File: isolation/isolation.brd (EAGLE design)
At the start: 74.5 x 72.7 mm, 90 parts, among them IC1 XTLV61048DBVR, IC2 SN74HC14PWR, IC3 SN74HCS32BQAR, IC4 SN74HCS08DYYR, IC5 FDN359BN, IC6 FDN359BN, IC7 FDN359BN, IC8 FDN359BN, J1 S4B-PH-K-S(LF)(SN), J2 S4B-PH-K-S(LF)(SN), J3 S2B-PH-K-S(LF)(SN), J4 S2B-PH-K-S(LF)(SN), J5 S2B-PH-K-S(LF)(SN), J6 USBC

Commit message: fix drc issues
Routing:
- net FIRE2: track 38.0 -> 39.7 mm
- net N$24: track 8.36 -> 7.42 mm
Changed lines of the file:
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@@
 <setting verticaltext="up"/>
 </settings>
-<grid distance="50" unitdist="mil" unit="mil" style="lines" multiple="1" display="no" altdistance="5" altunitdist="mil" altunit="mil"/>
+<grid distance="1" unitdist="mm" unit="mm" style="lines" multiple="1" display="no" altdistance="0.1" altunitdist="mm" altunit="mm"/>
 <layers>
 <layer number="1" name="Top" color="4" fill="1" visible="yes" active="yes"/>
@@
 <text x="5" y="-33" size="3" layer="22" font="vector" ratio="15" rot="MR0">Lockie</text>
 <text x="14.969" y="10.376" size="2" layer="22" font="vector" ratio="15" rot="MR0">Designed by ART Avionics</text>
-<text x="12.029" y="12.595" size="1.5" layer="22" font="vector" ratio="15" rot="MR0">Shrey Bohra</text>
+<text x="11.029" y="12.595" size="1.1" layer="22" font="vector" ratio="15" rot="MR0">Shrey Bohra</text>
 <text x="11.358" y="14.786" size="1" layer="22" font="vector" ratio="15" rot="MR0">Shreya Ramteke Sharwa Molla</text>
 <text x="3.598" y="16.306" size="1" layer="22" font="vector" ratio="15" rot="MR0">Abhik Chatterjee</text>
 <text x="4.066" y="18.493" size="1" layer="22" font="vector" ratio="15" rot="MR0">Camillo De Gregorio</text>
-<text x="-0.346" y="12.728" size="1" layer="22" font="vector" ratio="15" rot="MR0">Simeon Charles</text>
+<text x="0.654" y="12.728" size="1" layer="22" font="vector" ratio="15" rot="MR0">Simeon Charles</text>
 <text x="-18.415" y="19.685" size="1" layer="22" font="vector" ratio="15" rot="MR0">GND</text>
 <text x="-21.971" y="17.018" size="1" layer="22" font="vector" ratio="15" rot="MR0">VCC</text>
@@
 <text x="31.75" y="3.175" size="1.5" layer="21" font="vector" ratio="15" rot="R270">USB C</text>
 <text x="2.794" y="-22.606" size="1" layer="21" font="vector" ratio="15">JLCJLCJLCJLC</text>
+<text x="16.03" y="-29.21" size="1" layer="22" font="vector" ratio="12" rot="MR0">VCC</text>
+<text x="-16.57294375" y="-18.11725" size="1" layer="22" font="vector" ratio="12" rot="MR60">Raven Input</text>
+<text x="14.758228125" y="-18.887253125" size="1" layer="22" font="vector" ratio="12" rot="MR120">Pickle Input</text>
 </plain>
 <attributes>
@@
 <wire x1="-19.7358" y1="21.8694" x2="-19.67" y2="21.861" width="0.1524" layer="16"/>
 <wire x1="-16.5354" y1="24.3586" x2="-16.51" y2="24.5236" width="0.1524" layer="1"/>
-<wire x1="-17.4244" y1="22.7584" x2="-18.3134" y2="21.8694" width="0.1524" layer="16"/>
-<wire x1="-17.4244" y1="23.4696" x2="-17.4244" y2="22.7584" width="0.1524" layer="16"/>
-<wire x1="-18.3134" y1="21.8694" x2="-18.37" y2="21.861" width="0.1524" layer="16"/>
+<wire x1="-18.1244" y1="22.7584" x2="-18.37" y2="22.5128" width="0.1524" layer="16"/>
+<wire x1="-18.37" y1="21.861" x2="-18.37" y2="22.5128" width="0.1524" layer="16"/>
+<wire x1="-17.9578" y1="24.003" x2="-18.1244" y2="23.8364" width="0.1524" layer="16"/>
+<wire x1="-18.1244" y1="23.8364" x2="-18.1244" y2="22.7584" width="0.1524" layer="16"/>
 <wire x1="-13.208" y1="19.177" x2="-12.7" y2="19.685" width="0.1524" layer="16"/>
 <wire x1="-12.7" y1="20.05555" x2="-12.7" y2="19.685" width="0.1524" layer="16"/>
@@
 <wire x1="-12.0904" y1="16.891" x2="-11.954" y2="16.778" width="0.1524" layer="16"/>
 <wire x1="-12.446" y1="16.891" x2="-12.454" y2="16.778" width="0.1524" layer="16"/>
-<wire x1="-17.9578" y1="24.003" x2="-17.4244" y2="23.4696" width="0.1524" layer="16"/>
 <wire x1="-19.0246" y1="23.2918" x2="-19.05" y2="23.25335" width="0.1524" layer="1"/>
 <wire x1="9.001" y1="5.08" x2="11.43" y2="7.62" width="0.1524" layer="16"/>
@@
 <wire x1="-12.0904" y1="12.9794" x2="-11.9126" y2="13.1572" width="0.1524" layer="16"/>
 <wire x1="-11.7348" y1="12.6238" x2="-12.0904" y2="12.9794" width="0.1524" layer="16"/>
-<wire x1="-12.446" y1="11.9126" x2="-11.9126" y2="12.446" width="0.1524" layer="16"/>
-<wire x1="-11.9126" y1="12.446" x2="-11.7348" y2="12.6238" width="0.1524" layer="16"/>
+<wire x1="-12.446" y1="11.9126" x2="-11.8626" y2="12.496" width="0.1524" layer="16"/>
+<wire x1="-11.8626" y1="12.496" x2="-11.7348" y2="12.6238" width="0.1524" layer="16"/>
 <wire x1="-15.113" y1="11.9126" x2="-13.97" y2="11.9126" width="0.1524" layer="16"/>
 <wire x1="-13.97" y1="11.9126" x2="-12.446" y2="11.9126" width="0.1524" layer="16"/>
@@
 <wire x1="-11.9126" y1="13.6906" x2="-11.954" y2="13.702" width="0.1524" layer="16"/>
 <wire x1="-32.5374" y1="8.1788" x2="-32.385" y2="8.348" width="0.1524" layer="1"/>
-<wire x1="-11.3792" y1="11.9126" x2="-11.9126" y2="12.446" width="0.1524" layer="16"/>
-<wire x1="-10.1346" y1="10.668" x2="-11.3792" y2="11.9126" width="0.1524" layer="1"/>
+<wire x1="-11.1792" y1="11.8126" x2="-11.8626" y2="12.496" width="0.1524" layer="16"/>
+<wire x1="-10.1346" y1="10.668" x2="-10.1346" y2="10.768" width="0.1524" layer="1"/>
+<wire x1="-10.1346" y1="10.768" x2="-11.1792" y2="11.8126" width="0.1524" layer="1"/>
 <wire x1="-10.1346" y1="7.3406" x2="-10.1346" y2="10.668" width="0.1524" layer="16"/>
 <wire x1="-10.1346" y1="7.112" x2="-10.1346" y2="7.3406" width="0.1524" layer="1"/>
@@
 <via x="-20.8026" y="17.78" extent="1-16" drill="0.35"/>
 <via x="-19.9136" y="18.669" extent="1-16" drill="0.35"/>
-<via x="-11.3792" y="11.9126" extent="1-16" drill="0.35"/>
+<via x="-11.1792" y="11.8126" extent="1-16" drill="0.35"/>
 <via x="-10.1346" y="10.668" extent="1-16" drill="0.35"/>
 <via x="-10.1346" y="7.3406" extent="1-16" drill="0.35"/>
@@
 <wire x1="-28.448" y1="8.1788" x2="-28.448" y2="8.348" width="0.1524" layer="1"/>
 <wire x1="-28.3972" y1="16.3576" x2="-28.448" y2="16.51" width="0.1524" layer="16"/>
-<wire x1="-12.8016" y1="9.779" x2="-11.7348" y2="9.779" width="0.1524" layer="1"/>
+<wire x1="-11.684" y1="9.8322" x2="-11.8016" y2="9.9498" width="0.1524" layer="1"/>
+<wire x1="-11.8016" y1="9.9498" x2="-11.8016" y2="11.079" width="0.1524" layer="1"/>
 <wire x1="-14.4018" y1="8.1788" x2="-13.335" y2="9.2456" width="0.1524" layer="16"/>
-<wire x1="-13.335" y1="9.2456" x2="-12.8016" y2="9.779" width="0.1524" layer="16"/>
+<wire x1="-13.485" y1="9.3956" x2="-11.8016" y2="11.079" width="0.1524" layer="16"/>
 <wire x1="-27.2034" y1="8.1788" x2="-14.4018" y2="8.1788" width="0.1524" layer="16"/>
-<wire x1="-11.7348" y1="9.779" x2="-11.684" y2="9.8322" width="0.1524" layer="1"/>
 <via x="-27.2034" y="7.0866" extent="1-16" drill="0.35"/>
-<via x="-12.8016" y="9.779" extent="1-16" drill="0.35"/>
+<via x="-11.8016" y="11.079" extent="1-16" drill="0.35"/>
 <wire x1="-14.0462" y1="12.9794" x2="-14.0462" y2="13.6906" width="0.1524" layer="16"/>
 <wire x1="-14.4018" y1="12.6238" x2="-14.0462" y2="12.9794" width="0.1524" layer="16"/>
@@
 <wire x1="-15.8242" y1="12.0904" x2="-15.2908" y2="12.6238" width="0.1524" layer="16"/>
 <wire x1="-15.8242" y1="11.7348" x2="-15.8242" y2="12.0904" width="0.1524" layer="16"/>
-<wire x1="-13.335" y1="9.2456" x2="-15.8242" y2="11.7348" width="0.1524" layer="16"/>
+<wire x1="-13.335" y1="9.2456" x2="-13.485" y2="9.3956" width="0.1524" layer="16"/>
+<wire x1="-13.485" y1="9.3956" x2="-15.8242" y2="11.7348" width="0.1524" layer="16"/>
 <wire x1="-14.0462" y1="13.6906" x2="-13.954" y2="13.702" width="0.1524" layer="16"/>
 </signal>
@@
 <contactref element="J6" pad="B5"/>
 <contactref element="R12" pad="1"/>
-<wire x1="27.66795" y1="6.78675" x2="27.9932" y2="7.112" width="0.1524" layer="1"/>
 <via x="26.416" y="5.207" extent="1-16" drill="0.35"/>
 <wire x1="26.416" y1="5.207" x2="26.797" y2="4.826" width="0.1524" layer="16"/>
@@
 <wire x1="28.28" y1="2.131" x2="28.181" y2="2.032" width="0.1524" layer="1"/>
 <wire x1="28.181" y1="2.032" x2="26.797" y2="2.032" width="0.1524" layer="1"/>
-<wire x1="27.9932" y1="7.112" x2="27.806196875" y2="6.924996875" width="0.1778" layer="1"/>
-<wire x1="27.9932" y1="6.4032" x2="26.797" y2="5.207" width="0.1778" layer="1"/>
-<wire x1="26.416" y1="5.207" x2="26.797" y2="5.207" width="0.1778" layer="1"/>
-<wire x1="27.9932" y1="6.4032" x2="27.9932" y2="7.112" width="0.1778" layer="1"/>
+<wire x1="26.416" y1="5.207" x2="27.9932" y2="6.7842" width="0.1778" layer="1"/>
+<wire x1="27.9932" y1="6.7842" x2="27.9932" y2="7.112" width="0.1778" layer="1"/>
 </signal>
 <signal name="N$25">
@@
 <wire x1="-11.0236" y1="21.5138" x2="-11.7348" y2="21.5138" width="0.1524" layer="16"/>
 <wire x1="-10.8458" y1="21.336" x2="-11.0236" y2="21.5138" width="0.1524" layer="16"/>
-<wire x1="-16.5354" y1="21.336" x2="-10.8458" y2="21.336" width="0.1524" layer="1"/>
+<wire x1="-11.0458" y1="21.536" x2="-10.8458" y2="21.336" width="0.1524" layer="1"/>
+<wire x1="-11.0458" y1="21.536" x2="-16.3354" y2="21.536" width="0.1524" layer="1"/>
 <wire x1="-17.1958" y1="21.7424" x2="-16.6624" y2="21.209" width="0.1524" layer="1"/>
 <wire x1="-17.1958" y1="27.9654" x2="-17.1958" y2="21.7424" width="0.1524" layer="16"/>
@@
 <wire x1="-17.7038" y1="19.1008" x2="-18.0594" y2="19.1008" width="0.1524" layer="16"/>
 <wire x1="-17.7038" y1="20.1676" x2="-17.7038" y2="19.1008" width="0.1524" layer="1"/>
-<wire x1="-16.5354" y1="21.336" x2="-16.6624" y2="21.209" width="0.1524" layer="1"/>
+<wire x1="-16.3354" y1="21.536" x2="-16.6624" y2="21.209" width="0.1524" layer="1"/>
 <wire x1="-16.6624" y1="21.209" x2="-17.7038" y2="20.1676" width="0.1524" layer="1"/>
 <wire x1="-19.7358" y1="16.002" x2="-19.67" y2="15.985" width="0.1524" layer="16"/>

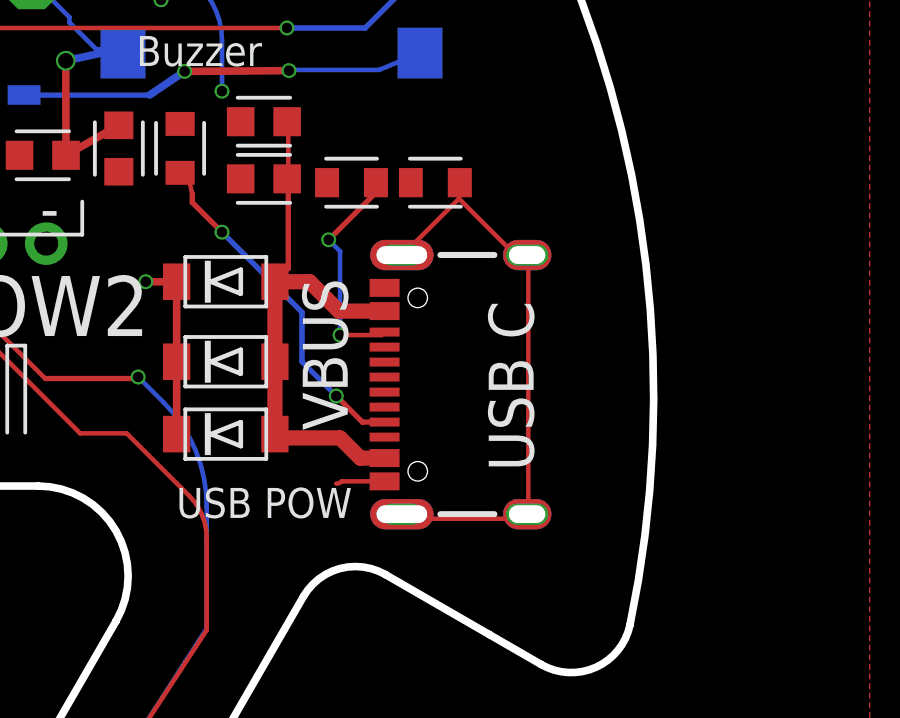
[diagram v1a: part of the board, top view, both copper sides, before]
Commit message: swap usb c connector
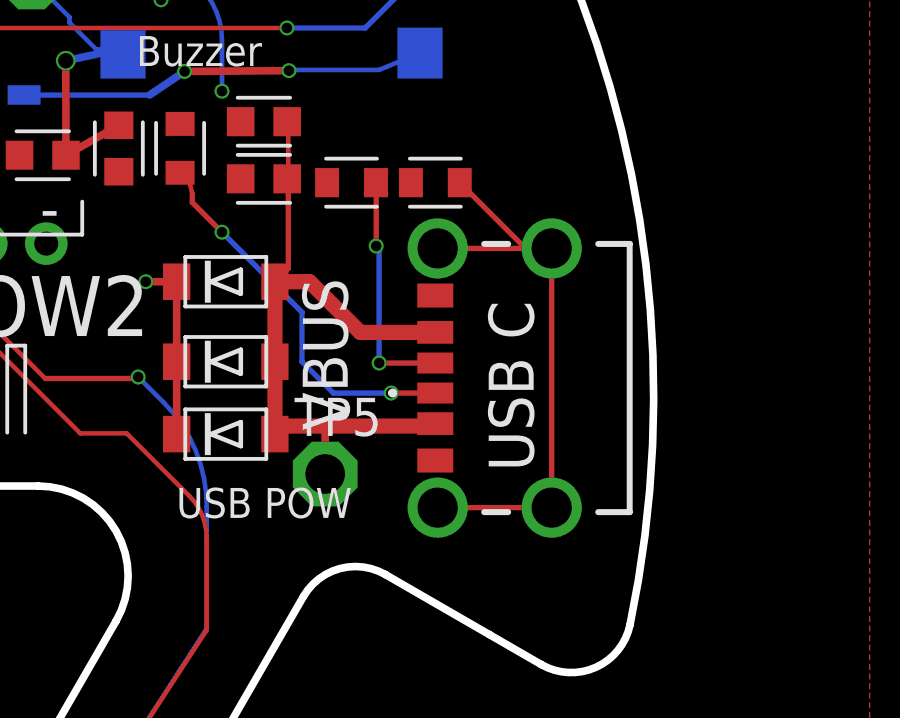
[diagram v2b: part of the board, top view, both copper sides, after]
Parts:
- removed J6: USBC, SparkFun-Connectors:USB-C-16P-2LAYER-PADS
- added J7: 217175-0001, SamacSys_Parts:2171750001
- added TP5: PTR1PAD1-13, testpad:P1-13
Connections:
- removed net N$21: J6.SHLD1, J6.SHLD2, J6.SHLD3, J6.SHLD4, R13.1
- removed net N$24: J6.B5, R12.1
- removed net N$25: J6.A5, R14.1
- removed net N$26: C14.2, C15.2, D2.A, D3.A, D4.A, J6.VBUS1, J6.VBUS2
- new net CC1: J7.A5, R14.1
- new net CC2: J7.B5, R12.1
- new net SHLD: J7.MH1, J7.MH2, J7.MH3, J7.MH4, R13.1
- new net VBUS: C14.2, C15.2, D2.A, D3.A, D4.A, J7.A9, J7.B9, TP5.TP
- net GND: now also J7.A12, J7.B12; no longer J6.GND, J6.GND2
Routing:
- net VBUS: track 0.00 -> 23.8 mm
- net SHLD: track 0.00 -> 19.3 mm
- net N$21: track 19.3 -> 0.00 mm
- net N$26: track 18.7 -> 0.00 mm
- net CC1: track 0.00 -> 12.8 mm, vias 0 -> 2
- net N$25: track 11.5 -> 0.00 mm, vias 2 -> 0
- net CC2: track 0.00 -> 7.93 mm, vias 0 -> 2
- net N$24: track 7.42 -> 0.00 mm, vias 2 -> 0
- net GND: track 84.2 -> 82.6 mm
